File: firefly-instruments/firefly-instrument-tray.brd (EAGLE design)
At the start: 193 x 100 mm, 155 parts, among them J1 CON-26, J10 CON-2CON-HEADER-2, J11 CON-2282847-2, J12 CON-2282847-2, J13 CON-1CT3151, J14 CON-1CT3151, J2 USB-4PINUSB-B1HSB6, J4 CON-26, J5 CON-26, J6 CON-10SWD, J7 CON-10SWD, J8 USB-4PINUSB-B1HSB6, J9 CON-10SWD, U10 PTC0603, U11:Q1 FET-NMCPH3, U11:U1 TXS2SA, U12 AP7331, U13 MCP47X6, U14 STM32F411-LQFP64, U1:C1 1uF, U1:J1 SMFLP, U1:R1 10k, U1:U1 TCS3471, U2:Q1 FET-NMCPH3, U2:U1 TXS2SA, U3:Q1 FET-NMCPH3, U3:U1 TXS2SA, U4:Q1 FET-NMCPH3, U4:U1 TXS2SA, U5:Q1 FET-NMCPH3, U5:U1 TXS2SA, U6:Q1 FET-NMCPH3, U6:U1 74LVCH1T45, U6:U2 74LVCH1T45, U7:Q1 FET-NMCPH3, U7:U1 74LVCH1T45, U7:U2 74LVCH1T45, U8:C1 1nF, U8:C2 100nF, U8:C3 10uF, U8:C4 1nF, U8:C7 1uF, U8:C9 100nF, U8:L1 1k, U8:L2 1k, U8:R1 1.8K, U8:R16 1, U8:R2 0, U8:R3 43, U8:R4 12K, U8:R5 10k, U8:R6 10k, U8:R7 376, U8:R8 1K, U8:U1 LTC6102-1MS8, U8:U2 TLV271SN2T1G, U9:C1 4700uF, U9:C10 1nF, U9:C11 100nF, U9:C12 10uF, U9:C13 1nF, U9:C14 1nF, U9:C15 100nF, U9:C16 1nF, U9:C17 1uF, U9:C18 100nF, U9:C19 100nF, U9:C2 100nF, U9:C3 100nF, U9:C4 1uF, U9:C5 1uF, U9:C6 10uF, U9:C7 4.7uF, U9:C8 510pF, U9:D1 D-USSOD-123A, U9:L1 22uH, U9:L2 1k, U9:L3 1k, U9:Q1 FET-NMCPH3, U9:R1 1K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

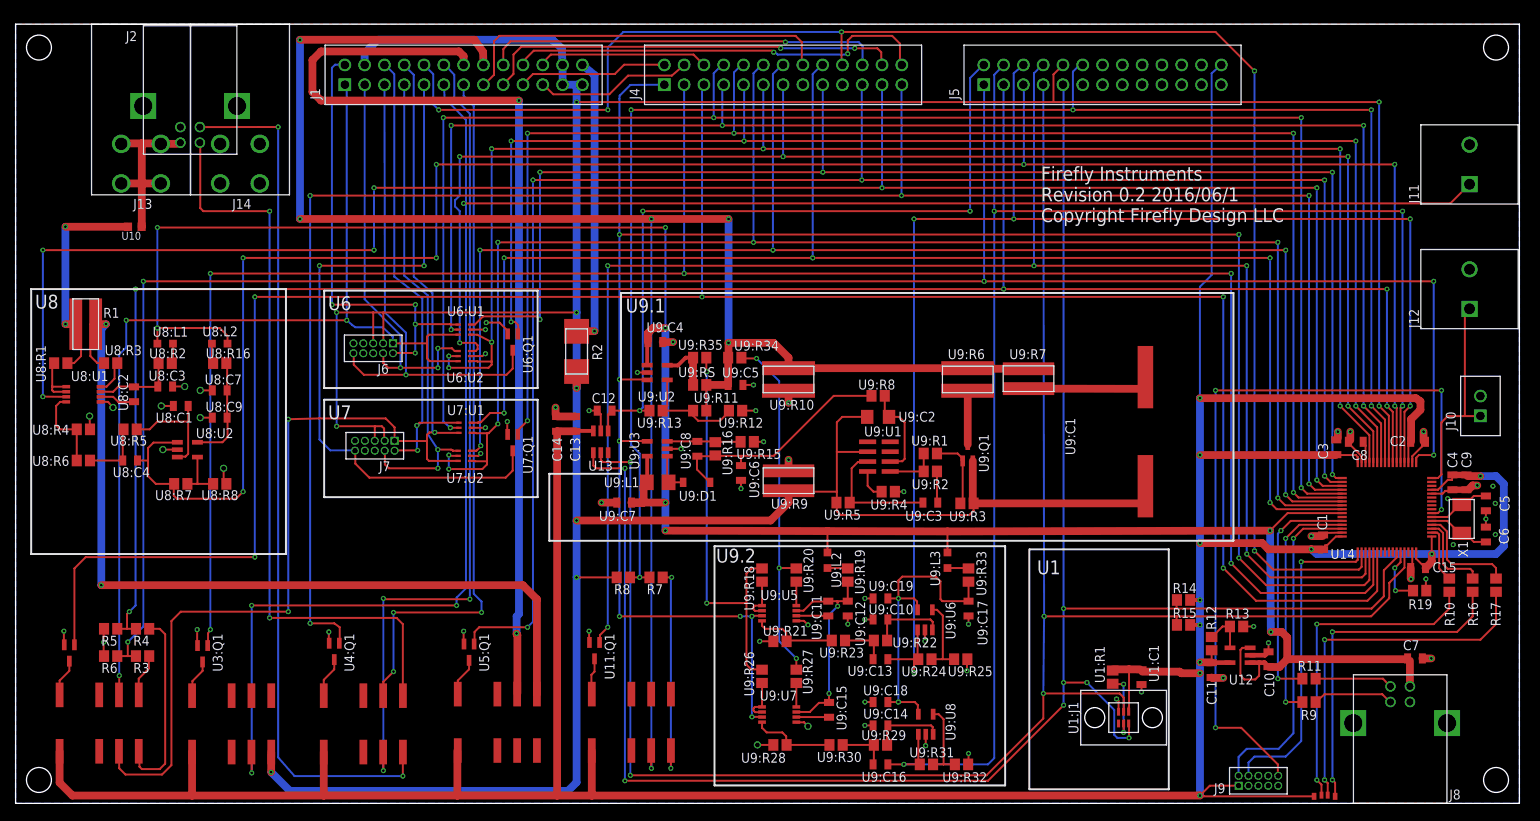
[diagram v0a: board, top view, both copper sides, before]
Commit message: Firefly Instrument Tray 0.3 (out for fab)
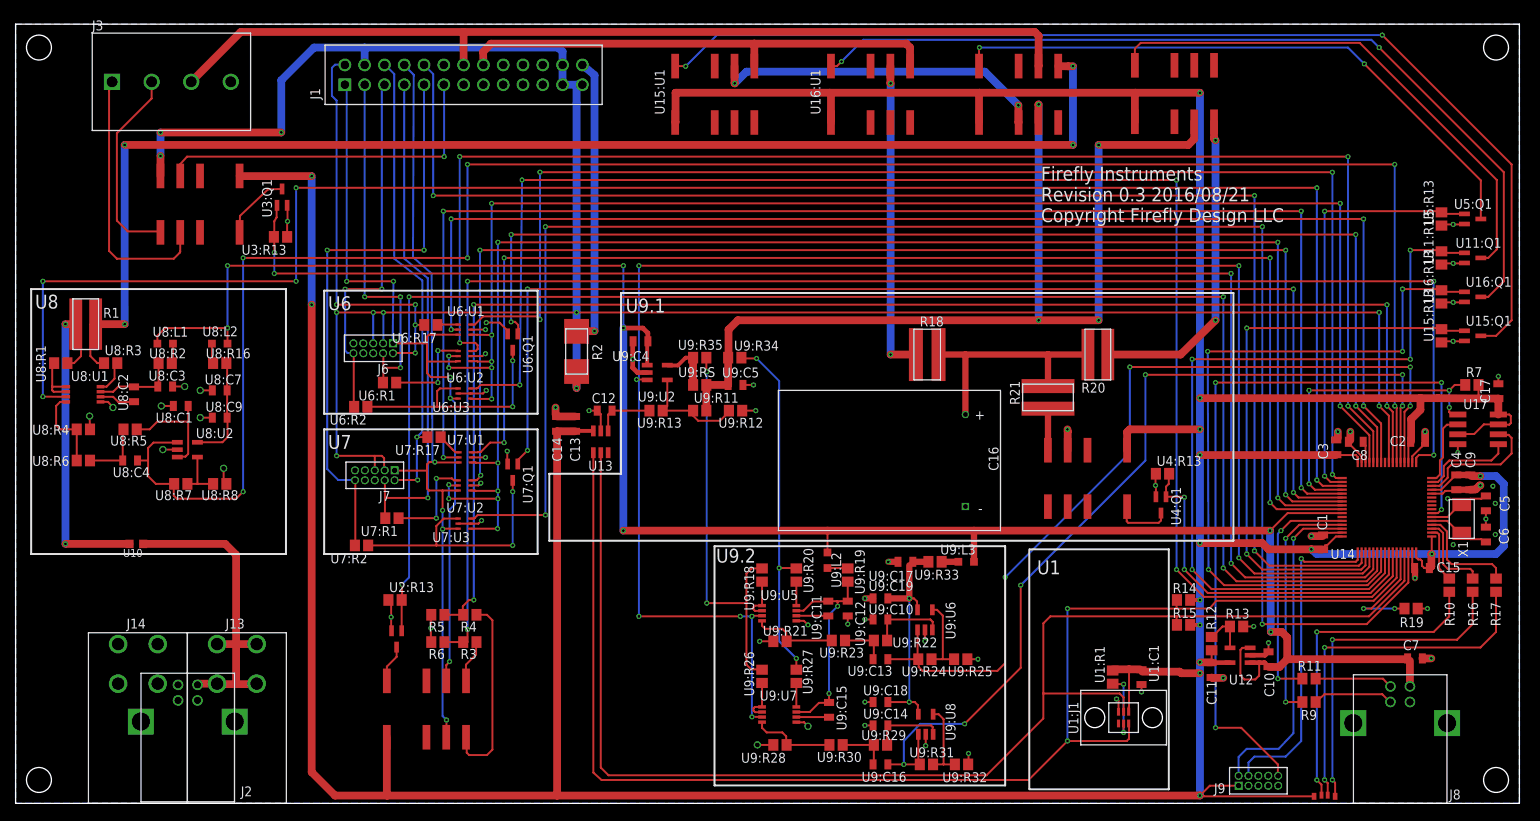
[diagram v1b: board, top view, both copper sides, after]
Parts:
- removed J10: CON-2CON-HEADER-2, firefly:CON-HEADER-2
- removed J11, J12: CON-2282847-2, firefly:282847-2
- removed J4, J5: CON-26, firefly:CON-HEADER-2X13
- removed R8: 1k, firefly:R0805
- removed U9:C1: 4700uF, firefly:EEVFK1A472M
- removed U9:C2: 100nF, firefly:C3216
- removed U9:C3: 100nF, firefly:C0805
- removed U9:C6: 10uF, firefly:C0805
- removed U9:C7: 4.7uF, firefly:C0805
- removed U9:C8: 510pF, firefly:C0805
- removed U9:D1: D-USSOD-123A, firefly:SOD-123A
- removed U9:L1: 22uH, firefly:L3225P
- removed U9:Q1: FET-NMCPH3, firefly:MCPH3
- removed U9:R1, U9:R4, U9:R5: 1K, firefly:R0805
- removed U9:R10: 200 (2W WW), firefly:RCL1225
- removed U9:R15: 36K, firefly:R0805
- removed U9:R16: 396K, firefly:R0805
- removed U9:R2: 10K, firefly:R0805
- removed U9:R3: 100K, firefly:R0805
- removed U9:R6: 1 (2W WW), firefly:RCL1225
- removed U9:R7, U9:R9: 0.1 (2W WW), firefly:KRL6432
- removed U9:R8: 10, firefly:R0805
- removed U9:U1: LT1078, firefly:SOIC8
- removed U9:U3: XC9119D10A, firefly:SOT-23-5
- added C16: 1F, firefly:PM118
- added C17: 100nF, firefly:C0805
- added J3: CON-4282847-4, firefly:282847-4
- added R18: 1 (2W WW), firefly:RCL1225
- added R20: 49.9 (2W WW), firefly:KRL6432
- added R21: 49.9 (2W WW), firefly:RCL1225
- added U11:R13, U15:R13, U16:R13, U2:R13, U3:R13, U4:R13, U5:R13: 10K, firefly:R0805
- added U15:Q1, U16:Q1: FET-NMCPH3, firefly:MCPH3
- added U15:U1, U16:U1: TXS2SA, firefly:TXS2SA
- added U17: MEMORY-SPISOA008, firefly:SOA008
- added U6:R1, U6:R17, U6:R2, U7:R1, U7:R17, U7:R2: 240, firefly:R0805
- added U6:U3, U7:U3: 74LVCH1T45, firefly:SOT363
- R7: value 1k -> 10k
- moved U5:Q1 140.3 mm to (187.0, 75.0), turned to 0 degrees
- moved U11:Q1 123.5 mm to (187.0, 70.0), turned to 0 degrees
- moved U4:Q1 107.8 mm to (147.0, 38.3)
- moved R7 107.6 mm to (186.9, 53.7), turned to 0 degrees
- moved U11:U1 106.6 mm to (150.0, 91.1)
- moved U5:U1 104.7 mm to (130.0, 91.0)
- moved U4:U1 95.7 mm to (136.3, 41.7), turned to 270 degrees
- moved J2 79.0 mm to (22.1, 10.5), turned to 0 degrees
- moved U3:U1 67.0 mm to (22.4, 76.9), turned to 270 degrees
- moved J14 65.5 mm to (15.7, 17.9), turned to 180 degrees
- moved J13 65.4 mm to (28.4, 17.9), turned to 180 degrees
- moved U3:Q1 59.5 mm to (34.2, 77.8), turned to 90 degrees
- moved R3 42.0 mm to (58.3, 20.7)
- moved R4 42.0 mm to (58.3, 24.2)
- moved R5 42.0 mm to (54.2, 24.2)
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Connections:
- removed net ATE_BATTERY+_SENSE: J5.8, U11:Q1.1, U14.51
- removed net ATE_USB_D_EN: J4.25, U14.36, U4:Q1.1
- removed net EXP_PA2: J10.1, J12.1, U14.16
- removed net N$21: J2.3, U4:U1.5
- removed net N$22: J2.2, U4:U1.8
- removed net U3:BC: U3:U1.9
- removed net U3:BNO: U3:U1.8
- removed net U5:AC: U5:U1.4
- removed net U5:ANC: U5:U1.3
- removed net U9:+12V: U9:C6.1, U9:C8.1, U9:D1.C, U9:R16.2, U9:R8.1
- removed net U9:N$1: U9:R1.1, U9:R2.2, U9:U1.5
- removed net U9:N$10: U9:Q1.3, U9:R6.1
- removed net U9:N$12: U9:D1.A, U9:L1.2, U9:U3.1
- removed net U9:N$2: U9:Q1.1, U9:R1.2, U9:R3.2
- removed net U9:N$3: U9:C3.1, U9:R2.1
- removed net U9:N$5: U9:R4.2, U9:U1.4
- removed net U9:N$6: U9:C8.2, U9:R15.2, U9:R16.1, U9:U3.3
- removed net U9:N$7: U9:C2.1, U9:R8.2, U9:U1.6
- removed net U9:N$8: U9:C3.2, U9:R5.2, U9:U1.3
- removed net U9:N$9: U9:C1.P, U9:R7.1
- new net ATE_BAT_ADJ_EN: U14.51, U15:Q1.1, U15:R13.2
- new net ATE_BAT_CAP_EN: U14.55, U16:Q1.1, U16:R13.2
- new net ATE_DRAIN_EN: U14.57, U4:Q1.1, U4:R13.2
- new net ATE_FILL_EN: U11:Q1.1, U11:R13.2, U14.56
- new net ATE_SWD1_SENSE_NRESET: U14.58, U6:U3.3
- new net ATE_SWD2_SENSE_NRESET: U14.62, U7:U3.3
- new net BATADJ: U11:U1.4, U5:U1.4, U9:C5.1, U9:R11.2, U9:R34.2, U9:RS.2
- new net BATADJSAFE: U15:U1.9, U5:U1.3
- new net BATCAP: R18.1, U16:U1.9
- new net DRAINCAP: R21.1, U4:U1.5
- new net DUT_SWITCH_1: J3.1, U3:U1.9
- new net DUT_SWITCH_2: J3.2, U3:U1.8
- new net FILLCAP: R20.1, U11:U1.5
- new net MEM_CSN: R7.1, U14.36, U17.1
- new net SPI_MISO: U14.16, U17.2
- new net SPI_MOSI: U14.15, U17.5
- new net SPI_SCLK: U14.14, U17.6
- new net U15:AC: U15:U1.4
- new net U15:ANC: U15:U1.3
- new net U15:ANO: U15:U1.5
- new net U15:BNC: U15:U1.10
- new net U15:N$2: U15:Q1.3, U15:U1.12
- new net U16:AC: U16:U1.4
- new net U16:ANC: U16:U1.3
- new net U16:ANO: U16:U1.5
- new net U16:BNC: U16:U1.10
- new net U16:N$2: U16:Q1.3, U16:U1.12
- new net U4:BC: U4:U1.9
- new net U4:BNO: U4:U1.8
- new net U6:N$1: U6:Q1.3, U6:R2.1, U6:U3.4
- new net U6:N$2: U6:R17.1, U6:U1.4
- new net U6:N$3: U6:R1.1, U6:U2.4
- new net U7:N$1: U7:Q1.3, U7:R2.1, U7:U3.4
- new net U7:N$2: U7:R17.1, U7:U1.4
- new net U7:N$3: U7:R1.1, U7:U2.4
- net +3V3: now also C17.1, R7.2, U15:U1.1, U16:U1.1, U17.3, U17.7, U17.8; no longer J5.26
- net ATE_BATTERY+2: no longer J5.12, R7.2, R8.1
- net ATE_BS_ADJ: no longer J5.2
- net ATE_BS_EN: no longer J4.1, U9:U3.4
- net ATE_BS_SHR: no longer J5.6
- net ATE_BS_SLR: no longer J5.4
- net ATE_BUTTON_EN: now also U3:R13.2; no longer J4.3
- net ATE_MCU1_VCC2: no longer J5.1
- net ATE_MCU2_VCC2: no longer J5.3
- net ATE_MCU_VCC_SENSE: now also U2:R13.2; no longer J4.5
- net ATE_SCL: no longer J5.7
- net ATE_SDA: no longer J5.9
- net ATE_SWD1_DIR_TO_DUT: no longer J4.7
- net ATE_SWD1_NRESET: no longer J4.9
- net ATE_SWD1_PWR: now also U6:U3.1; no longer J4.11
- net ATE_SWD1_SWDCLK: no longer J4.13
- net ATE_SWD1_SWDIO: no longer J4.17
- net ATE_SWD2_DIR_TO_DUT: no longer J4.8
- net ATE_SWD2_NRESET: no longer J4.10
- net ATE_SWD2_PWR: now also U7:U3.1; no longer J4.12
- net ATE_SWD2_SWDCLK: no longer J4.14
- net ATE_SWD2_SWDIO: no longer J4.18
- net ATE_USB_5V_EN: now also U5:R13.2; no longer J4.21
- net ATE_USB_CS_EN: no longer J4.23
- net ATE_USB_CS_OUT: no longer J5.5
- net DUT_BATTERY+: now also U15:U1.8, U16:U1.8; no longer U11:U1.4, U9:C5.1, U9:R10.2, U9:R11.2, U9:R34.2, U9:R6.2, U9:R7.2, U9:RS.2
- net DUT_BUTTON+: no longer J11.1
- net DUT_GND: no longer J5.10, R8.2, U9:C1.M, U9:C2.2, U9:Q1.2, U9:R3.1, U9:R5.1, U9:R9.2, U9:U1.2
- net DUT_I2C_DRDY: no longer J4.22
- net DUT_I2C_SCL: no longer J4.26
- net DUT_I2C_SDA: no longer J4.24
- net DUT_MCU1_NRESET: now also U6:R2.2; no longer U6:Q1.3
- net DUT_MCU1_SWDCLK: now also U6:R1.2; no longer U6:U2.4
- net DUT_MCU1_SWDIO: now also U6:R17.2; no longer U6:U1.4
- net DUT_MCU1_VCC: now also U6:U3.6
- net DUT_MCU2_BOOT0: no longer J4.20
- net DUT_MCU2_NRESET: now also U7:R2.2; no longer U7:Q1.3
- net DUT_MCU2_SWDCLK: now also U7:R1.2; no longer U7:U2.4
- net DUT_MCU2_SWDIO: now also U7:R17.2; no longer U7:U1.4
- net DUT_MCU2_VCC: now also U7:U3.6
- net DUT_SPI_MISO: no longer J4.6
- net DUT_SPI_MOSI: no longer J4.4
- net DUT_SPI_SCLK: no longer J4.2
- net DUT_USB_5V: now also J3.3
- net DUT_USB_D+: no longer U4:U1.4
- net DUT_USB_D-: no longer U4:U1.9
- net DUT_VB: no longer J4.16
- net GND: now also C16.-, C17.2, J3.4, U11:R13.1, U15:Q1.2, U15:R13.1, U16:Q1.2, U16:R13.1, U17.4, U2:R13.1, U3:R13.1, U4:R13.1, U4:U1.4, U5:R13.1, U6:U3.2, U6:U3.5, U7:U3.2, U7:U3.5; no longer J10.2, J11.2, J12.2, J4.15, J4.19, U9:C6.2, U9:C7.2, U9:R10.1, U9:R15.1, U9:R4.1, U9:R9.1, U9:U3.2
- net N$4: now also C16.+, R18.2, R20.2, R21.2; no longer R7.1, U11:U1.5
- net USB_VBUS: no longer U9:C7.1, U9:L1.1, U9:U3.5
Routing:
- net ATE_USB_D_EN: track 244.9 -> 0.00 mm, vias 5 -> 0
- net ATE_SWD2_SENSE_NRESET: track 0.00 -> 214.6 mm, vias 0 -> 4
- net ATE_BATTERY+_SENSE: track 213.8 -> 0.00 mm, vias 5 -> 0
- net ATE_BATTERY+2: track 210.5 -> 0.00 mm, vias 5 -> 0
- net DUT_BUTTON+: track 249.3 -> 45.1 mm, vias 4 -> 1
- net ATE_SWD1_SENSE_NRESET: track 0.00 -> 200.2 mm, vias 0 -> 4
- net DUT_BATTERY+: track 244.8 -> 62.4 mm, vias 6 -> 0
- net ATE_USB_5V_EN: track 220.7 -> 54.7 mm, vias 5 -> 2
- net DUT_GND: track 498.2 -> 332.9 mm, vias 10 -> 11
- net +3V3: track 495.2 -> 643.9 mm, vias 11 -> 15
- net U15:N$2: track 0.00 -> 140.7 mm, vias 0 -> 2
- net BATADJ: track 0.00 -> 128.5 mm, vias 0 -> 4
- net U16:N$2: track 0.00 -> 112.6 mm, vias 0 -> 2
- net N$21: track 111.1 -> 0.00 mm, vias 2 -> 0
- net DUT_USB_D+: track 105.6 -> 0.00 mm, vias 3 -> 0
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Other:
- board text added: "Firefly Instruments Revision 0.3 2016/08/21 Copyright Firefly Design LLC"
- board text removed: "Firefly Instruments Revision 0.2 2016/06/1 Copyright Firefly Design LLC"

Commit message: Rev 0.4 instrument board - ready for production
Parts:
- added U9:R1: 0, firefly:R0805
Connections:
- net DUT_GND: now also U9:R1.2
- net GND: now also U9:R1.1
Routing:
- net DUT_GND: track 332.9 -> 330.2 mm
- net GND: track 139.3 -> 140.8 mm, vias 65 -> 66
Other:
- board text added: "Firefly Instruments Revision 0.4 2016/09/13 Copyright Firefly Design LLC"
- board text removed: "Firefly Instruments Revision 0.3 2016/08/21 Copyright Firefly Design LLC"

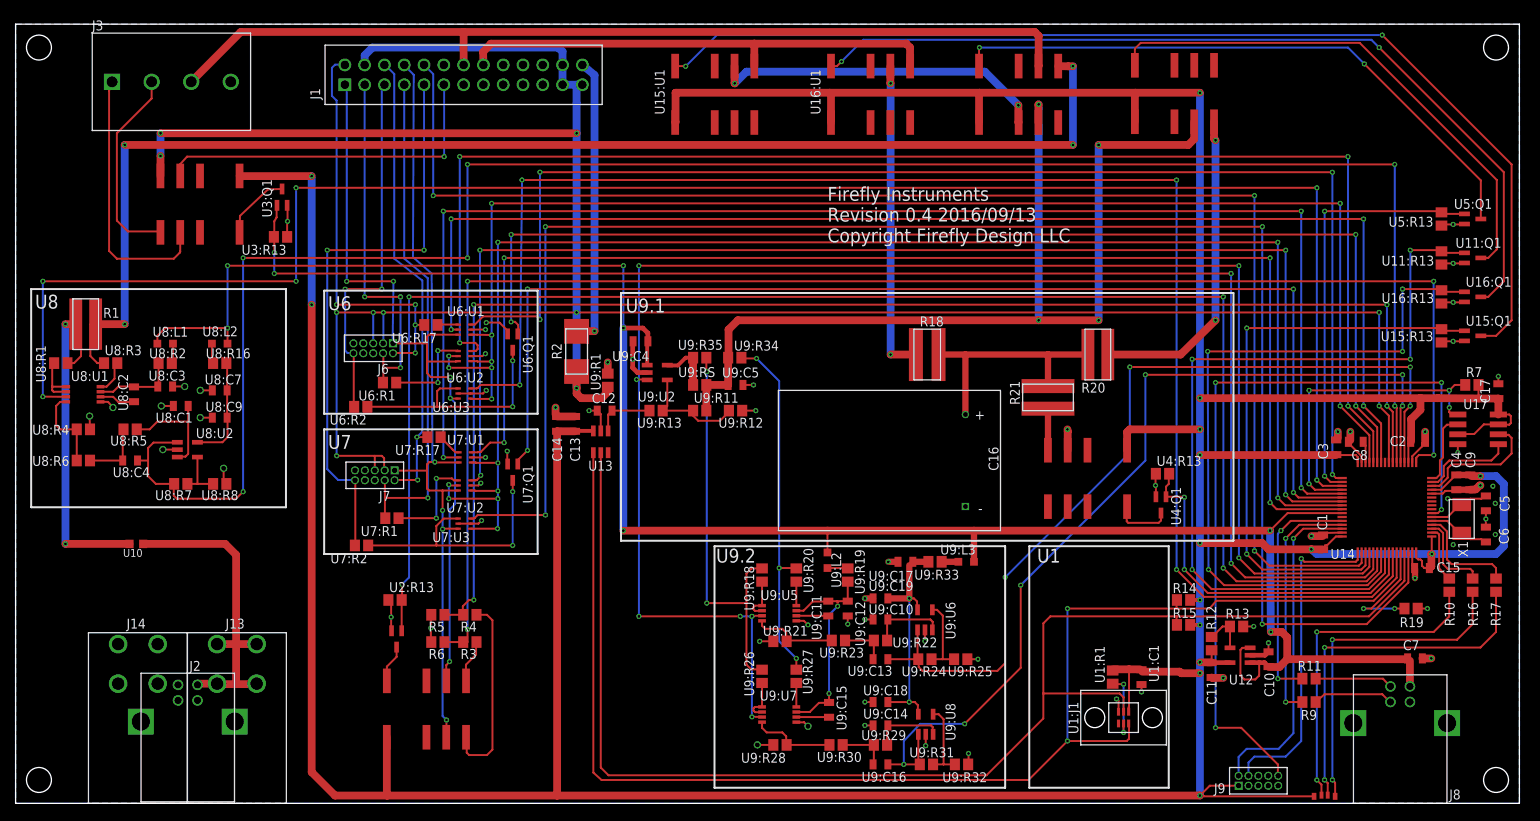
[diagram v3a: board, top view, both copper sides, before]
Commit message: add battery simulator voltage to A/D; separate motor minus from ground; remove J2; bump to version 0.5
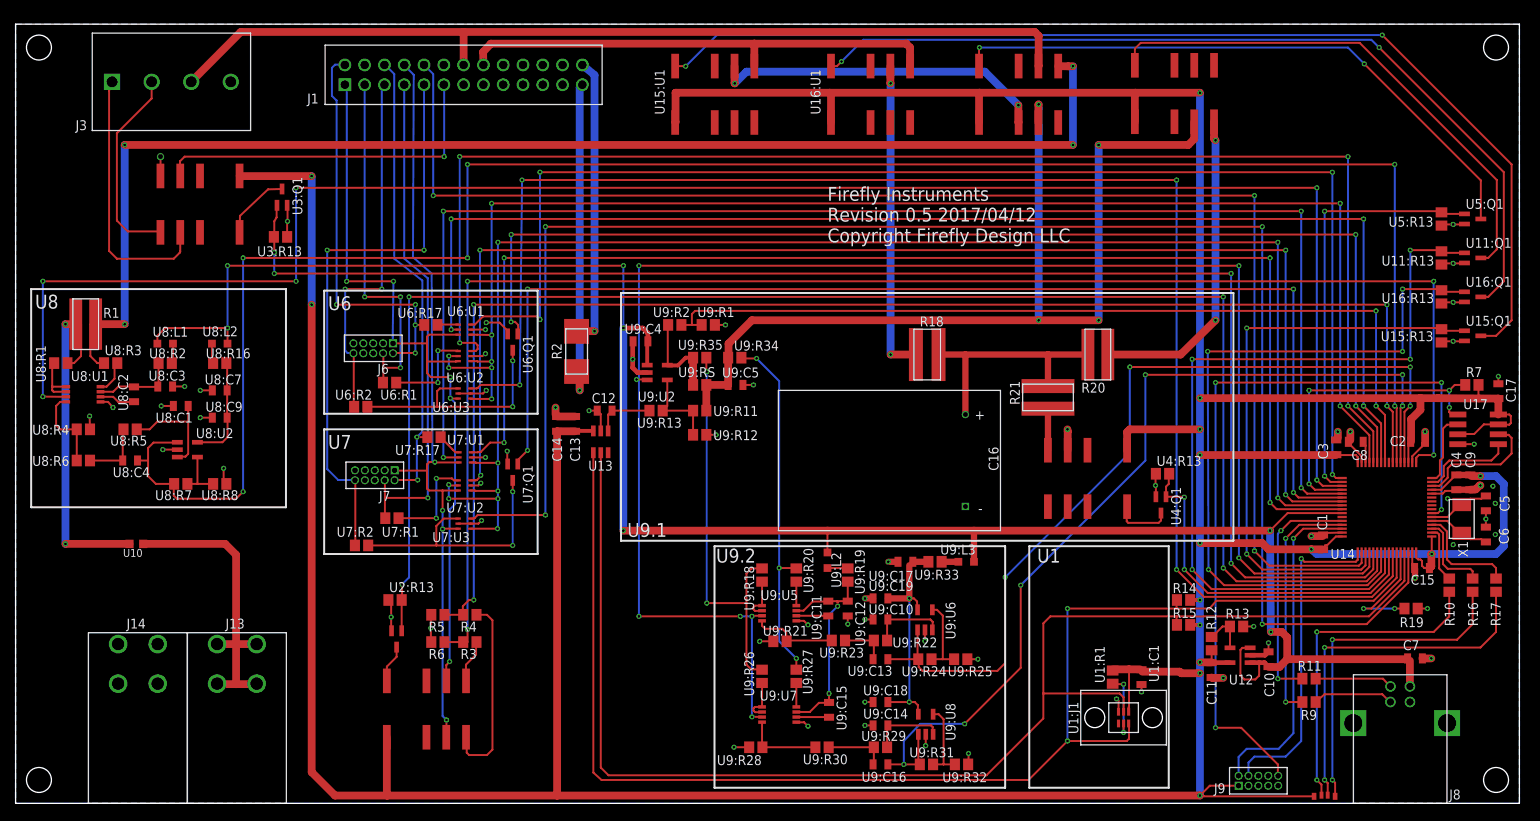
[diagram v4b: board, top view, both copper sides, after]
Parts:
- removed J2: USB-4PINUSB-B1HSB6, firefly:USB-B1HSB6
- added U9:R2: 100K, firefly:R0805
- U9:R1: value 0 -> 100K
- moved U9:R1 14.7 mm to (88.9, 61.4), turned to 180 degrees
- moved U9:R12 5.55 mm to (87.8, 47.3)
- moved U9:R28 3.11 mm to (95.0, 7.20)
- moved U9:R30 1.82 mm to (103.5, 7.20)
- moved U9:R29 0.30 mm to (111.0, 7.20)
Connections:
- removed net DUT_GND: J1.23, J1.24, J1.25, J1.4, J6.3, J6.5, J7.3, J7.5, R2.2, U14.24, U3:U1.5, U9:R1.2
- new net DUT_MOTOR-: J1.25, R2.2
- net +5V: no longer J2.1
- net ATE_BATTERY+2: now also U9:R1.2, U9:R2.1
- net GND: now also J1.23, J1.24, J1.4, J6.3, J6.5, J7.3, J7.5, U3:U1.5; no longer J2.4
- net U9:N$35: now also U9:R2.2
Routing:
- net DUT_GND: track 330.2 -> 0.00 mm, vias 11 -> 0
- net ATE_BATTERY+2: track 0.00 -> 111.9 mm, vias 0 -> 2
- net DUT_MOTOR-: track 0.00 -> 42.0 mm, vias 0 -> 1
- net U9:N$35: track 7.24 -> 12.4 mm
- net U9:N$4: track 14.3 -> 11.2 mm
- net GND: track 140.8 -> 143.6 mm, vias 66 -> 67
- net +5V: track 42.0 -> 39.4 mm
- net U9:N$25: track 6.54 -> 8.04 mm
- net BATADJ: track 128.5 -> 127.5 mm
- net U9:N$24: track 10.9 -> 10.0 mm
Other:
- board text added: "Firefly Instruments Revision 0.5 2017/04/12 Copyright Firefly Design LLC"
- board text removed: "Firefly Instruments Revision 0.4 2016/09/13 Copyright Firefly Design LLC"

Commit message: revision 0.5 ready for production
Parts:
- U12, U9:U2: value AP7331 -> VREG-ADJAP7331-WG-7
- X1: value XTAL2TXC_7A -> XTAL2CX5032GA; device firefly:TXC_7A -> firefly:CX5032GA
